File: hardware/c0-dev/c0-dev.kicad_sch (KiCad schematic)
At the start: 27 parts, among them J101 2913730000, J102 2913730000, J103 2913730000, J104 2913730000, J105 2913730000, J106 2913730000, J107 2913730000, J108 2913730000, J109 2913730000, J110 2913730000, J111 2913730000, J112 2913730000

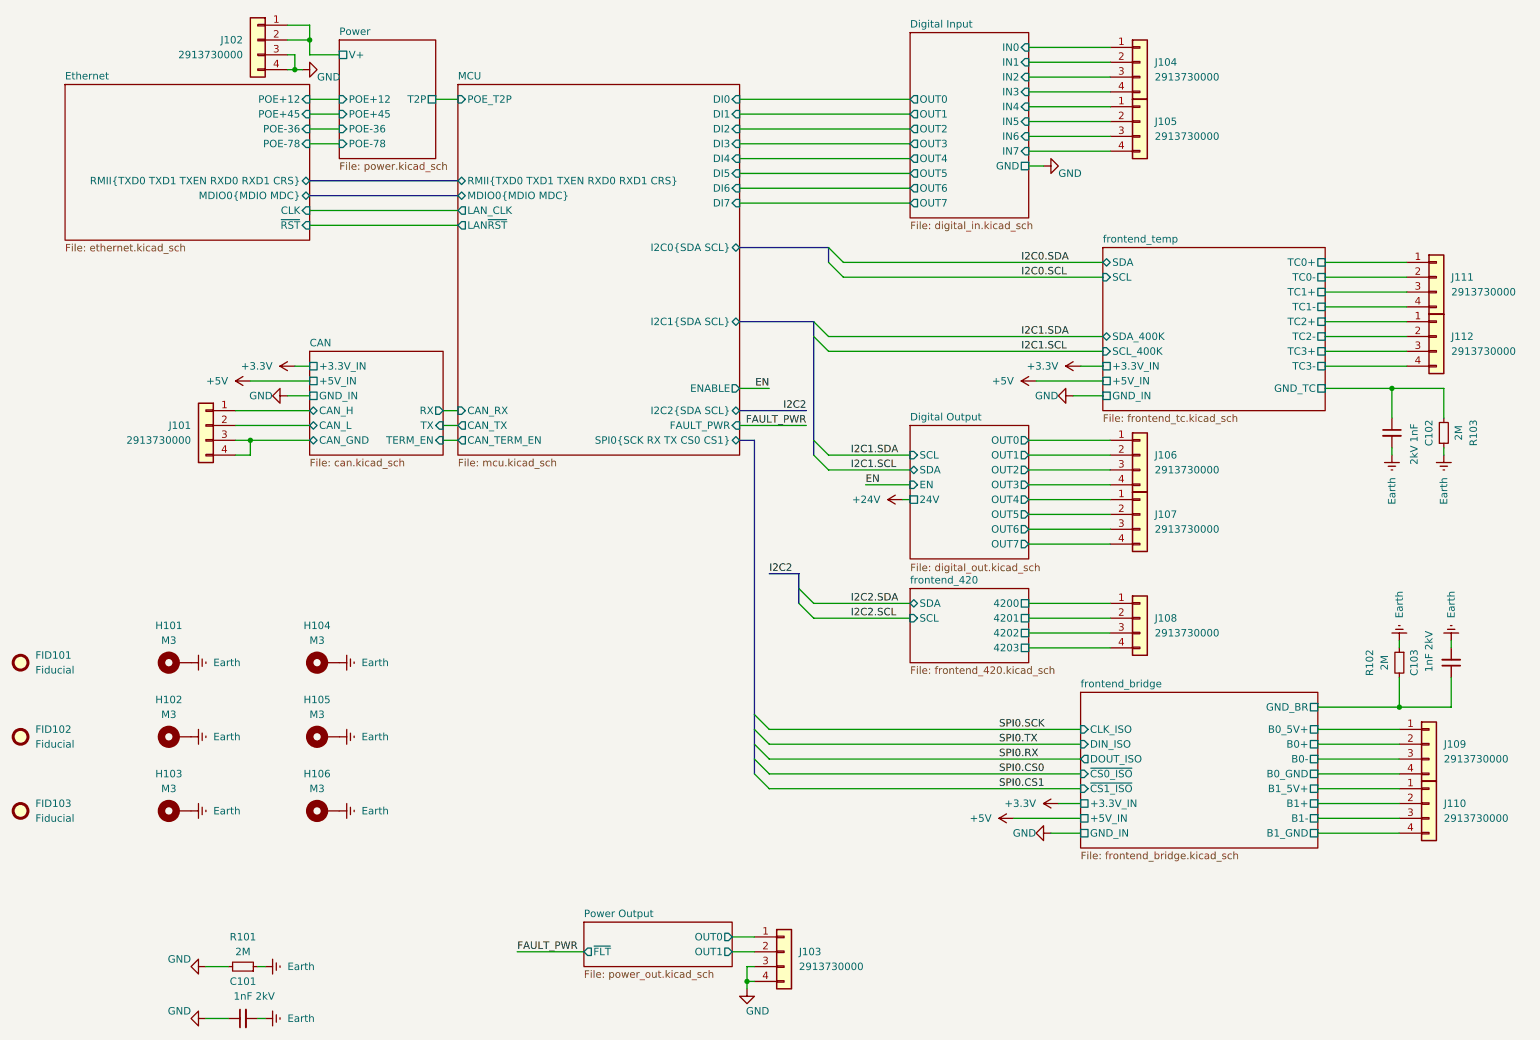
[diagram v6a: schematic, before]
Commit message: inital placement done
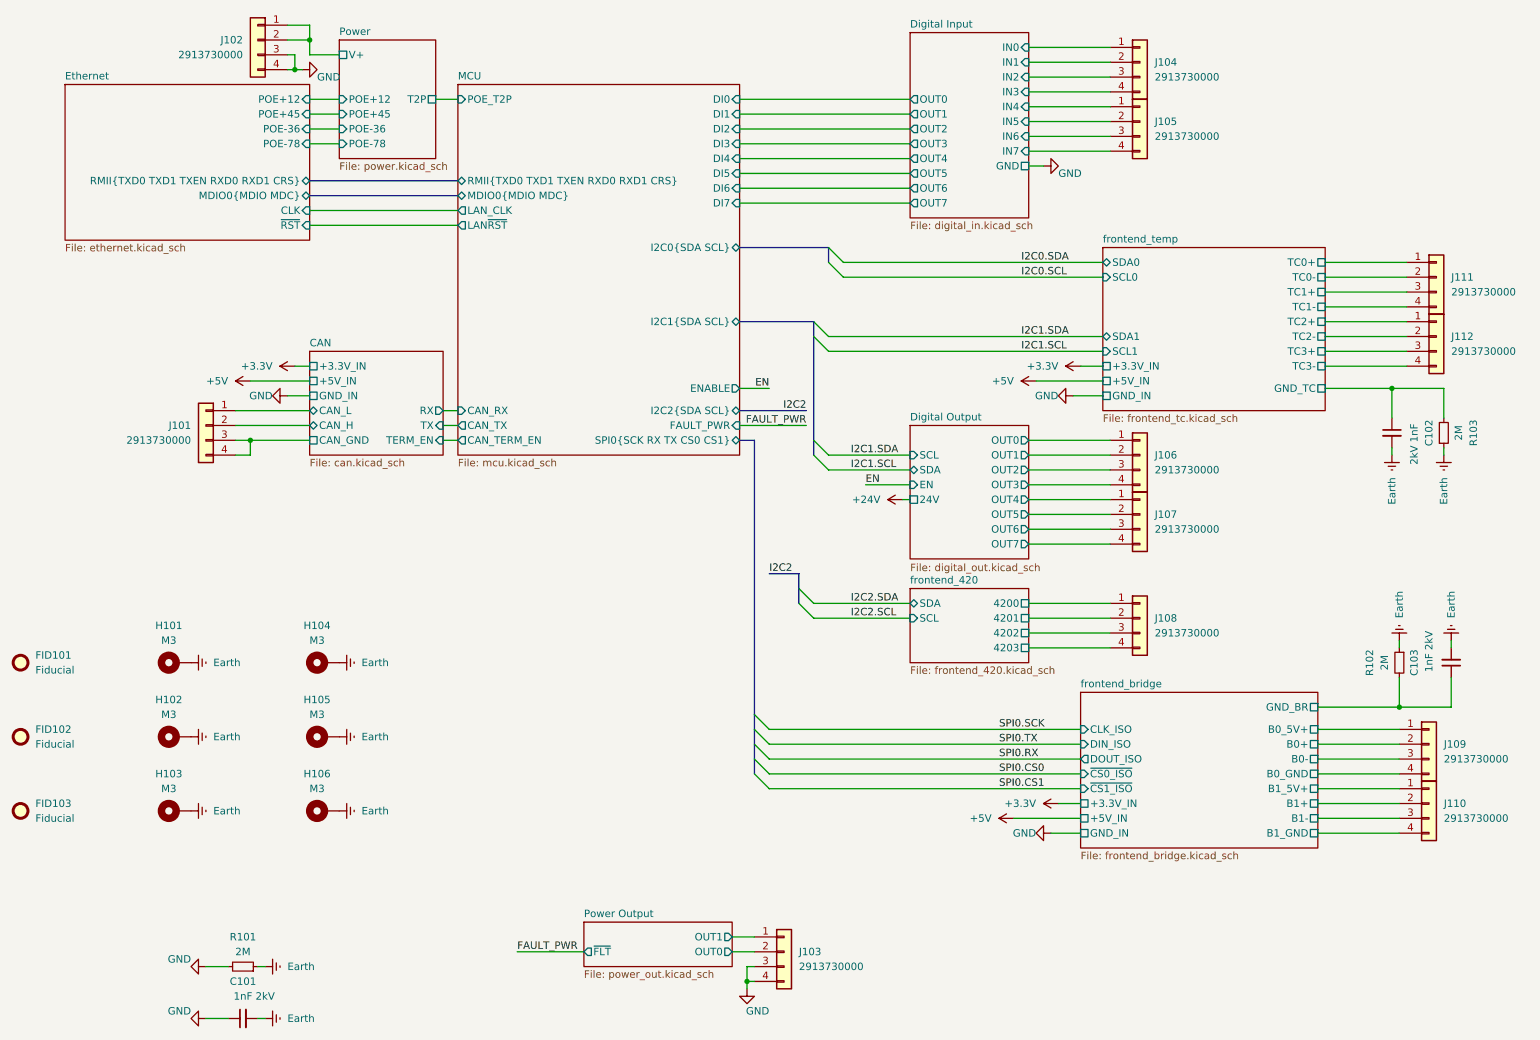
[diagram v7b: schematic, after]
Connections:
- net CAN/CAN_H: now also J101.2 (Pin_2); no longer J101.1 (Pin_1)
- net CAN/CAN_L: now also J101.1 (Pin_1); no longer J101.2 (Pin_2)
- net Power Output/OUT0: now also J103.2 (Pin_2); no longer J103.1 (Pin_1)
- net Power Output/OUT1: now also J103.1 (Pin_1); no longer J103.2 (Pin_2)
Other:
- sheet frontend_temp ports: added SCL0, SCL1, SDA0, SDA1; removed SCL, SCL_400K, SDA, SDA_400K
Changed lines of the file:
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@@
 	(wire
 		(pts
-			(xy 147.32 176.53) (xy 151.13 176.53)
-		)
-		(stroke
-			(width 0)
-			(type default)
-		)
-	)
-	(wire
-		(pts
 			(xy 148.59 48.26) (xy 177.8 48.26)
 		)
@@
 	(wire
 		(pts
-			(xy 74.93 38.1) (xy 80.01 38.1)
+			(xy 62.23 86.36) (xy 74.93 86.36)
 		)
 		(stroke
@@
 	(wire
 		(pts
-			(xy 121.92 176.53) (xy 110.49 176.53)
+			(xy 74.93 38.1) (xy 80.01 38.1)
 		)
 		(stroke
@@
 	(wire
 		(pts
-			(xy 198.12 104.14) (xy 212.09 104.14)
+			(xy 121.92 176.53) (xy 110.49 176.53)
 		)
 		(stroke
@@
 	(wire
 		(pts
-			(xy 74.93 30.48) (xy 80.01 30.48)
+			(xy 198.12 104.14) (xy 212.09 104.14)
 		)
 		(stroke
@@
 	(wire
 		(pts
-			(xy 62.23 83.82) (xy 74.93 83.82)
+			(xy 74.93 30.48) (xy 80.01 30.48)
 		)
 		(stroke
@@
 		)
 	)
-	(wire
-		(pts
-			(xy 62.23 86.36) (xy 74.93 86.36)
-		)
-		(stroke
-			(width 0)
-			(type default)
-		)
-	)
 	(bus
 		(pts
@@
 	(wire
 		(pts
+			(xy 62.23 83.82) (xy 74.93 83.82)
+		)
+		(stroke
+			(width 0)
+			(type default)
+		)
+	)
+	(wire
+		(pts
 			(xy 148.59 35.56) (xy 177.8 35.56)
 		)
@@
 	(wire
 		(pts
+			(xy 147.32 176.53) (xy 151.13 176.53)
+		)
+		(stroke
+			(width 0)
+			(type default)
+		)
+	)
+	(wire
+		(pts
 			(xy 270.51 124.46) (xy 270.51 123.19)
 		)
@@
 	(wire
 		(pts
-			(xy 147.32 173.99) (xy 151.13 173.99)
-		)
-		(stroke
-			(width 0)
-			(type default)
-		)
-	)
-	(wire
-		(pts
 			(xy 97.79 86.36) (xy 100.33 86.36)
 		)
@@
 	(wire
 		(pts
+			(xy 147.32 173.99) (xy 151.13 173.99)
+		)
+		(stroke
+			(width 0)
+			(type default)
+		)
+	)
+	(wire
+		(pts
 			(xy 198.12 96.52) (xy 212.09 96.52)
 		)
@@
 			)
 		)
-		(pin "CAN_GND" bidirectional
+		(pin "CAN_GND" passive
 			(at 74.93 88.9 180)
 			(effects
@@
 		)
 		(pin "CAN_H" bidirectional
-			(at 74.93 83.82 180)
+			(at 74.93 86.36 180)
 			(effects
 				(font
@@
 		)
 		(pin "CAN_L" bidirectional
-			(at 74.93 86.36 180)
+			(at 74.93 83.82 180)
 			(effects
 				(font
@@
 			)
 		)
-		(pin "SDA" bidirectional
-			(at 210.82 58.42 180)
-			(effects
-				(font
-					(size 1.27 1.27)
-				)
-				(justify left)
-			)
-		)
-		(pin "SCL" input
-			(at 210.82 60.96 180)
-			(effects
-				(font
-					(size 1.27 1.27)
-				)
-				(justify left)
-			)
-		)
 		(pin "TC1+" passive
 			(at 248.92 63.5 0)
@@
 			)
 		)
-		(pin "SCL_400K" input
-			(at 210.82 73.66 180)
+		(pin "+3.3V_IN" passive
+			(at 210.82 76.2 180)
 			(effects
 				(font
@@
 			)
 		)
-		(pin "SDA_400K" bidirectional
-			(at 210.82 71.12 180)
+		(pin "GND_IN" passive
+			(at 210.82 81.28 180)
 			(effects
 				(font
@@
 			)
 		)
-		(pin "+3.3V_IN" passive
-			(at 210.82 76.2 180)
+		(pin "GND_TC" passive
+			(at 248.92 80.01 0)
+			(effects
+				(font
+					(size 1.27 1.27)
+				)
+				(justify right)
+			)
+		)
+		(pin "+5V_IN" passive
+			(at 210.82 78.74 180)
 			(effects
 				(font
@@
 			)
 		)
-		(pin "GND_IN" passive
-			(at 210.82 81.28 180)
+		(pin "SCL1" input
+			(at 210.82 73.66 180)
 			(effects
 				(font
@@
 			)
 		)
-		(pin "GND_TC" passive
-			(at 248.92 80.01 0)
+		(pin "SDA0" bidirectional
+			(at 210.82 58.42 180)
 			(effects
 				(font
 					(size 1.27 1.27)
 				)
-				(justify right)
+				(justify left)
 			)
 		)
-		(pin "+5V_IN" passive
-			(at 210.82 78.74 180)
+		(pin "SCL0" input
+			(at 210.82 60.96 180)
+			(effects
+				(font
+					(size 1.27 1.27)
+				)
+				(justify left)
+			)
+		)
+		(pin "SDA1" bidirectional
+			(at 210.82 71.12 180)
 			(effects
 				(font
@@
 		)
 		(pin "OUT1" output
-			(at 147.32 176.53 0)
+			(at 147.32 173.99 0)
 			(effects
 				(font
@@
 		)
 		(pin "OUT0" output
-			(at 147.32 173.99 0)
+			(at 147.32 176.53 0)
 			(effects
 				(font
